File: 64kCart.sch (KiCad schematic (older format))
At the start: 9 parts, among them SW1 SW_Push, U1 27C512, U2 74LS173, U3 74LS04, U4 C64-Exp-Port

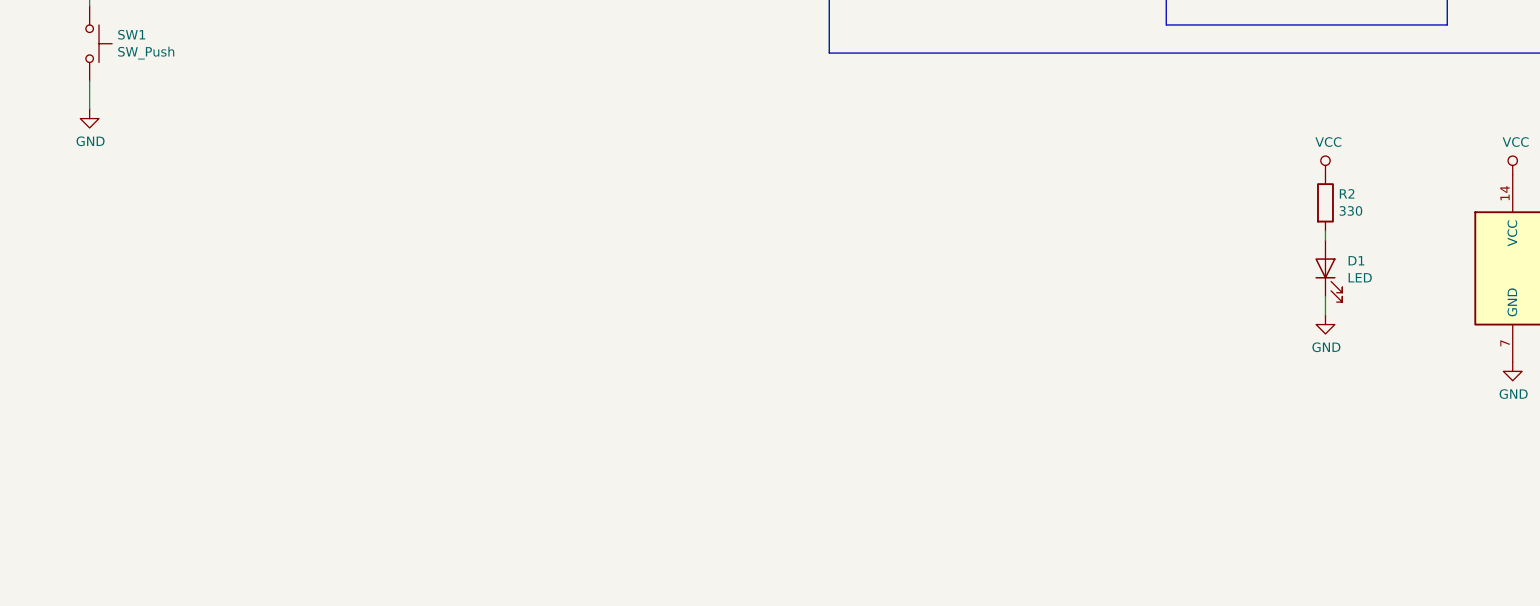
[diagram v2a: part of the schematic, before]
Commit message: Some work on board layout.
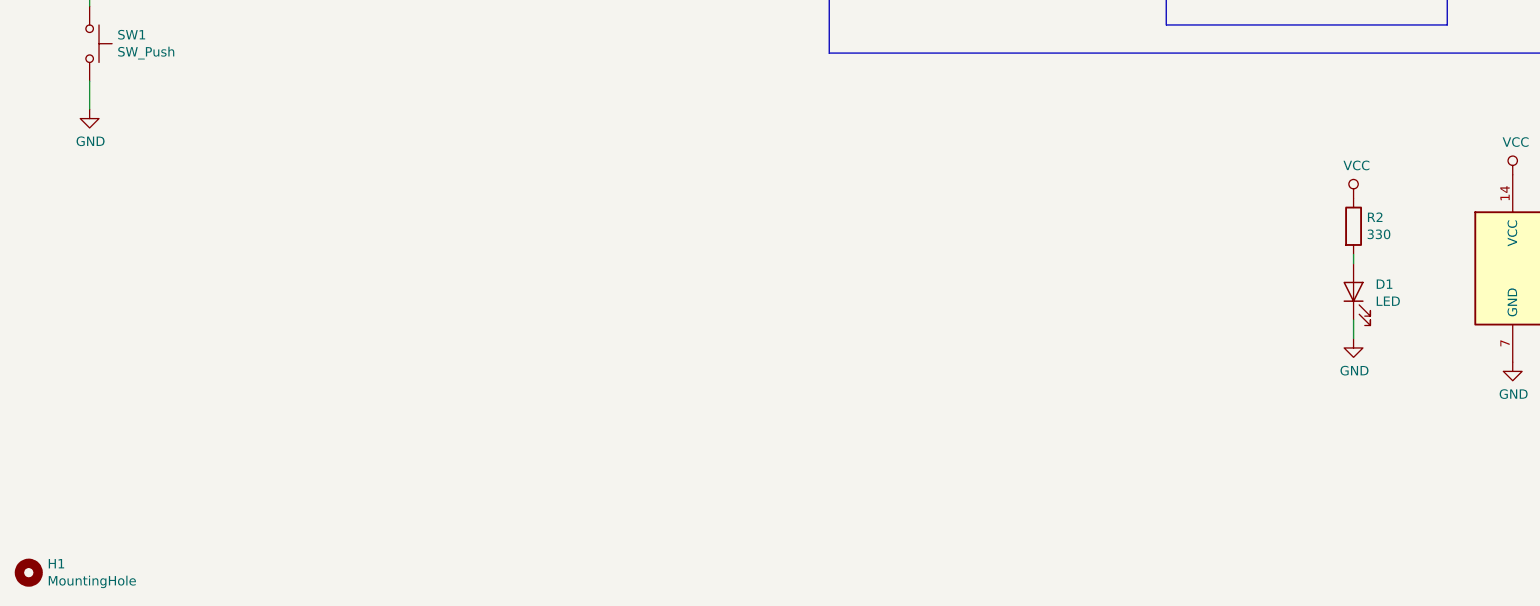
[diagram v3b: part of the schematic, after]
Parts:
- added H1: MountingHole, Mounting_Holes:MountingHole_5mm, symbol Mechanical:MountingHole
- D1: footprint LEDs:LED_D5.0mm -> LEDs:LED_D3.0mm
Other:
- moved on the sheet: D1, R2
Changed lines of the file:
@@
 encoding utf-8
 Sheet 1 1
-Title ""
+Title "64k Cart Remix"
 Date ""
-Rev ""
-Comp ""
-Comment1 ""
-Comment2 ""
-Comment3 ""
+Rev "Rev.1"
+Comp "hackup.net"
+Comment1 "Based on the original \"64k Karte\" design by Hucky"
+Comment2 "Creative Commons Attribution-NonCommercial-ShareAlike 4.0 International License."
+Comment3 "This work is licensed under a"
 Comment4 ""
 $EndDescr
@@
 L device:R R2
 U 1 1 5CE6B617
-P 7800 5400
-F 0 "R2" H 7870 5446 50  0000 L CNN
-F 1 "330" H 7870 5355 50  0000 L CNN
-F 2 "Resistors_THT:R_Axial_DIN0207_L6.3mm_D2.5mm_P7.62mm_Horizontal" V 7730 5400 50  0001 C CNN
-F 3 "~" H 7800 5400 50  0001 C CNN
-	1    7800 5400
+P 7950 5525
+F 0 "R2" H 8020 5571 50  0000 L CNN
+F 1 "330" H 8020 5480 50  0000 L CNN
+F 2 "Resistors_THT:R_Axial_DIN0207_L6.3mm_D2.5mm_P7.62mm_Horizontal" V 7880 5525 50  0001 C CNN
+F 3 "~" H 7950 5525 50  0001 C CNN
+	1    7950 5525
 	1    0    0    -1
 $EndComp
@@
 L power:VCC #PWR0116
 U 1 1 5CE6BAE1
-P 7800 5250
-F 0 "#PWR0116" H 7800 5100 50  0001 C CNN
-F 1 "VCC" H 7817 5423 50  0000 C CNN
-F 2 "" H 7800 5250 50  0001 C CNN
-F 3 "" H 7800 5250 50  0001 C CNN
-	1    7800 5250
+P 7950 5375
+F 0 "#PWR0116" H 7950 5225 50  0001 C CNN
+F 1 "VCC" H 7967 5548 50  0000 C CNN
+F 2 "" H 7950 5375 50  0001 C CNN
+F 3 "" H 7950 5375 50  0001 C CNN
+	1    7950 5375
 	1    0    0    -1
 $EndComp
@@
 L device:LED D1
 U 1 1 5CE72C00
-P 7800 5750
-F 0 "D1" V 7839 5633 50  0000 R CNN
-F 1 "LED" V 7748 5633 50  0000 R CNN
-F 2 "LEDs:LED_D5.0mm" H 7800 5750 50  0001 C CNN
-F 3 "~" H 7800 5750 50  0001 C CNN
-	1    7800 5750
+P 7950 5875
+F 0 "D1" V 7989 5758 50  0000 R CNN
+F 1 "LED" V 7898 5758 50  0000 R CNN
+F 2 "LEDs:LED_D3.0mm" H 7950 5875 50  0001 C CNN
+F 3 "~" H 7950 5875 50  0001 C CNN
+	1    7950 5875
 	0    -1   -1   0
 $EndComp
@@
 L power:GND #PWR0117
 U 1 1 5CE7311F
-P 7800 6000
-F 0 "#PWR0117" H 7800 5750 50  0001 C CNN
-F 1 "GND" H 7805 5827 50  0000 C CNN
-F 2 "" H 7800 6000 50  0001 C CNN
-F 3 "" H 7800 6000 50  0001 C CNN
-	1    7800 6000
-	1    0    0    -1
-$EndComp
-Wire Wire Line
-	7800 5600 7800 5550
-Wire Wire Line
-	7800 6000 7800 5900
+P 7950 6125
+F 0 "#PWR0117" H 7950 5875 50  0001 C CNN
+F 1 "GND" H 7955 5952 50  0000 C CNN
+F 2 "" H 7950 6125 50  0001 C CNN
+F 3 "" H 7950 6125 50  0001 C CNN
+	1    7950 6125
+	1    0    0    -1
+$EndComp
+Wire Wire Line
+	7950 5725 7950 5675
+Wire Wire Line
+	7950 6125 7950 6025
 $Comp
 L Switch:SW_Push SW1
@@
 Wire Wire Line
 	4600 2600 4600 3050
+$Comp
+L Mechanical:MountingHole H1
+U 1 1 5CD49171
+P 875 7375
+F 0 "H1" H 975 7421 50  0000 L CNN
+F 1 "MountingHole" H 975 7330 50  0000 L CNN
+F 2 "Mounting_Holes:MountingHole_5mm" H 875 7375 50  0001 C CNN
+F 3 "~" H 875 7375 50  0001 C CNN
+	1    875  7375
+	1    0    0    -1
+$EndComp
 Wire Bus Line
 	1850 1350 1850 2800

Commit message: First layout completed.
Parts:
- H1: footprint Mounting_Holes:MountingHole_5mm -> 64kCart:MountingHole_CartCombined
- SW1: value SW_Push -> Reset
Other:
- moved on the sheet: H1
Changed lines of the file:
@@
 P 1200 4550
 F 0 "SW1" V 1154 4698 50  0000 L CNN
-F 1 "SW_Push" V 1245 4698 50  0000 L CNN
+F 1 "Reset" V 1245 4698 50  0000 L CNN
 F 2 "Buttons_Switches_THT:SW_Tactile_SPST_Angled_PTS645Vx83-2LFS" H 1200 4750 50  0001 C CNN
 F 3 "~" H 1200 4750 50  0001 C CNN
@@
 L Mechanical:MountingHole H1
 U 1 1 5CD49171
-P 875 7375
-F 0 "H1" H 975 7421 50  0000 L CNN
-F 1 "MountingHole" H 975 7330 50  0000 L CNN
-F 2 "Mounting_Holes:MountingHole_5mm" H 875 7375 50  0001 C CNN
-F 3 "~" H 875 7375 50  0001 C CNN
-	1    875  7375
+P 950 7350
+F 0 "H1" H 1050 7396 50  0000 L CNN
+F 1 "MountingHole" H 1050 7305 50  0000 L CNN
+F 2 "64kCart:MountingHole_CartCombined" H 950 7350 50  0001 C CNN
+F 3 "~" H 950 7350 50  0001 C CNN
+	1    950  7350
 	1    0    0    -1
 $EndComp
